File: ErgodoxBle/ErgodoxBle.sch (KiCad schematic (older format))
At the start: 86 parts, among them K0 KEYSW, K1 KEYSW, K10 KEYSW, K11 KEYSW, K12 KEYSW, K13 KEYSW, K14 KEYSW, K15 KEYSW, K16 KEYSW, K2 KEYSW, K20 KEYSW, K21 KEYSW, K22 KEYSW, K23 KEYSW, K24 KEYSW, K25 KEYSW, K26 KEYSW, K3 KEYSW, K30 KEYSW, K31 KEYSW, K32 KEYSW, K33 KEYSW, K34 KEYSW, K35 KEYSW, K36 KEYSW, K4 KEYSW, K40 KEYSW, K41 KEYSW, K42 KEYSW, K43 KEYSW, K44 KEYSW, K45 KEYSW, K46 KEYSW, K5 KEYSW, K54 KEYSW, K55 KEYSW, K56 KEYSW, K6 KEYSW, SW1 SW_PUSH, SW2 SW_PUSH

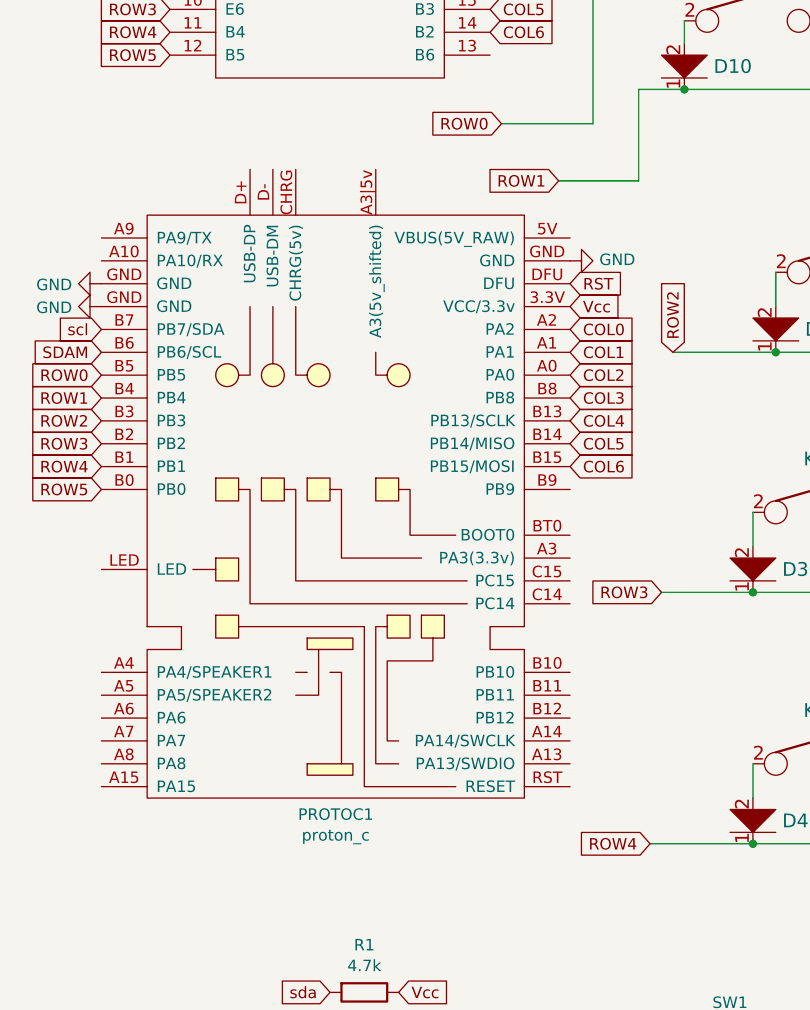
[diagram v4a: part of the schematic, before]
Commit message: added clearence for ProtonC
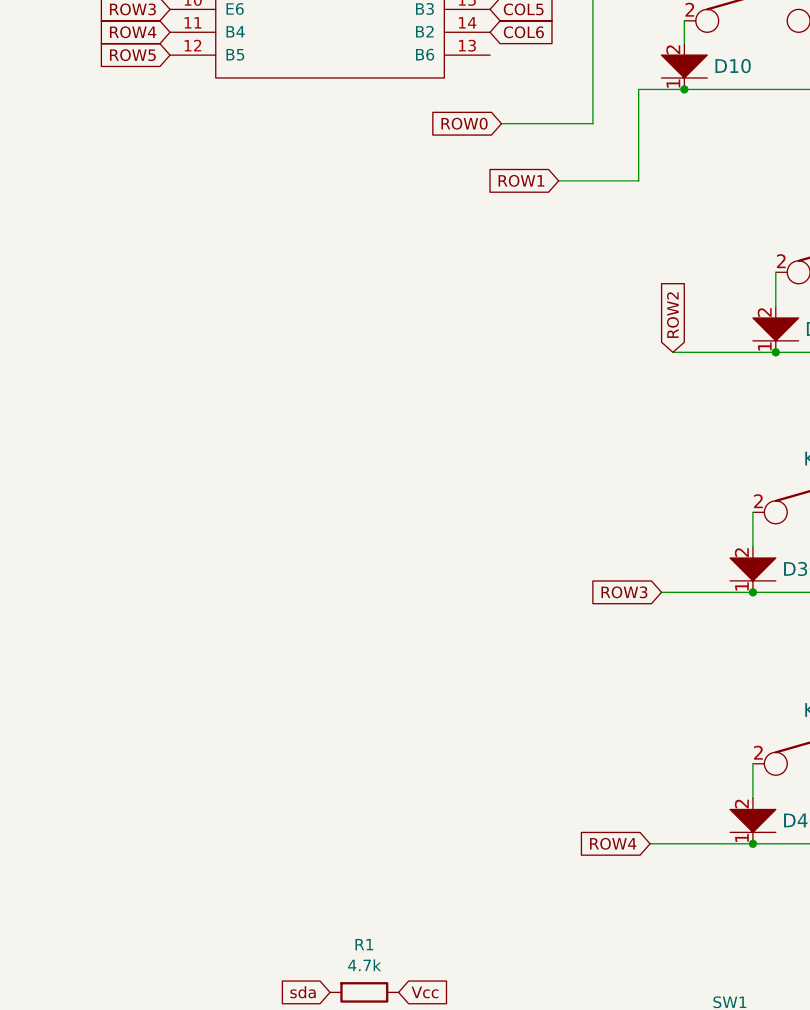
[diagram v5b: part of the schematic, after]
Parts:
- removed PROTOC1: proton_c, protonc:proton_c, symbol proton_c:proton_c
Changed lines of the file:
@@
 Text GLabel 10450 3900 0    50   Input ~ 0
 SDAM
-$Comp
-L proton_c:proton_c PROTOC1
-U 1 1 5C456AFA
-P 1550 3650
-F 0 "PROTOC1" H 1525 2128 50  0000 C CNN
-F 1 "proton_c" H 1525 2037 50  0000 C CNN
-F 2 "protonc:proton_c" H 1400 3650 50  0001 C CNN
-F 3 "" H 1400 3650 50  0001 C CNN
-	1    1550 3650
-	1    0    0    -1
-$EndComp
-Text GLabel 500  3250 0    50   Input ~ 0
-ROW0
-Text GLabel 500  3350 0    50   Input ~ 0
-ROW1
-Text GLabel 500  3450 0    50   Input ~ 0
-ROW2
-Text GLabel 500  3550 0    50   Input ~ 0
-ROW3
-Text GLabel 500  3650 0    50   Input ~ 0
-ROW4
-Text GLabel 500  3750 0    50   Input ~ 0
-ROW5
-Text GLabel 2550 3050 2    50   Input ~ 0
-COL0
-Text GLabel 2550 3150 2    50   Input ~ 0
-COL1
-Text GLabel 2550 3250 2    50   Input ~ 0
-COL2
-Text GLabel 2550 3350 2    50   Input ~ 0
-COL3
-Text GLabel 2550 3450 2    50   Input ~ 0
-COL4
-Text GLabel 2550 3550 2    50   Input ~ 0
-COL5
-Text GLabel 2550 3650 2    50   Input ~ 0
-COL6
-Text GLabel 2550 2850 2    50   Input ~ 0
-RST
-Text GLabel 2550 2950 2    50   Input ~ 0
-Vcc
-Text GLabel 500  3150 0    50   Input ~ 0
-SDAM
-Text GLabel 500  3050 0    50   Input ~ 0
-scl
-$Comp
-L power:GND #PWR0107
-U 1 1 5C45843C
-P 2550 2750
-F 0 "#PWR0107" H 2550 2500 50  0001 C CNN
-F 1 "GND" V 2555 2622 50  0000 R CNN
-F 2 "" H 2550 2750 50  0001 C CNN
-F 3 "" H 2550 2750 50  0001 C CNN
-	1    2550 2750
-	0    -1   -1   0
-$EndComp
-$Comp
-L power:GND #PWR0108
-U 1 1 5C45F50C
-P 500 2850
-F 0 "#PWR0108" H 500 2600 50  0001 C CNN
-F 1 "GND" V 505 2722 50  0000 R CNN
-F 2 "" H 500 2850 50  0001 C CNN
-F 3 "" H 500 2850 50  0001 C CNN
-	1    500  2850
-	0    1    1    0
-$EndComp
-$Comp
-L power:GND #PWR0109
-U 1 1 5C47B2A2
-P 500 2950
-F 0 "#PWR0109" H 500 2700 50  0001 C CNN
-F 1 "GND" V 505 2822 50  0000 R CNN
-F 2 "" H 500 2950 50  0001 C CNN
-F 3 "" H 500 2950 50  0001 C CNN
-	1    500  2950
-	0    1    1    0
-$EndComp
 $EndSCHEMATC

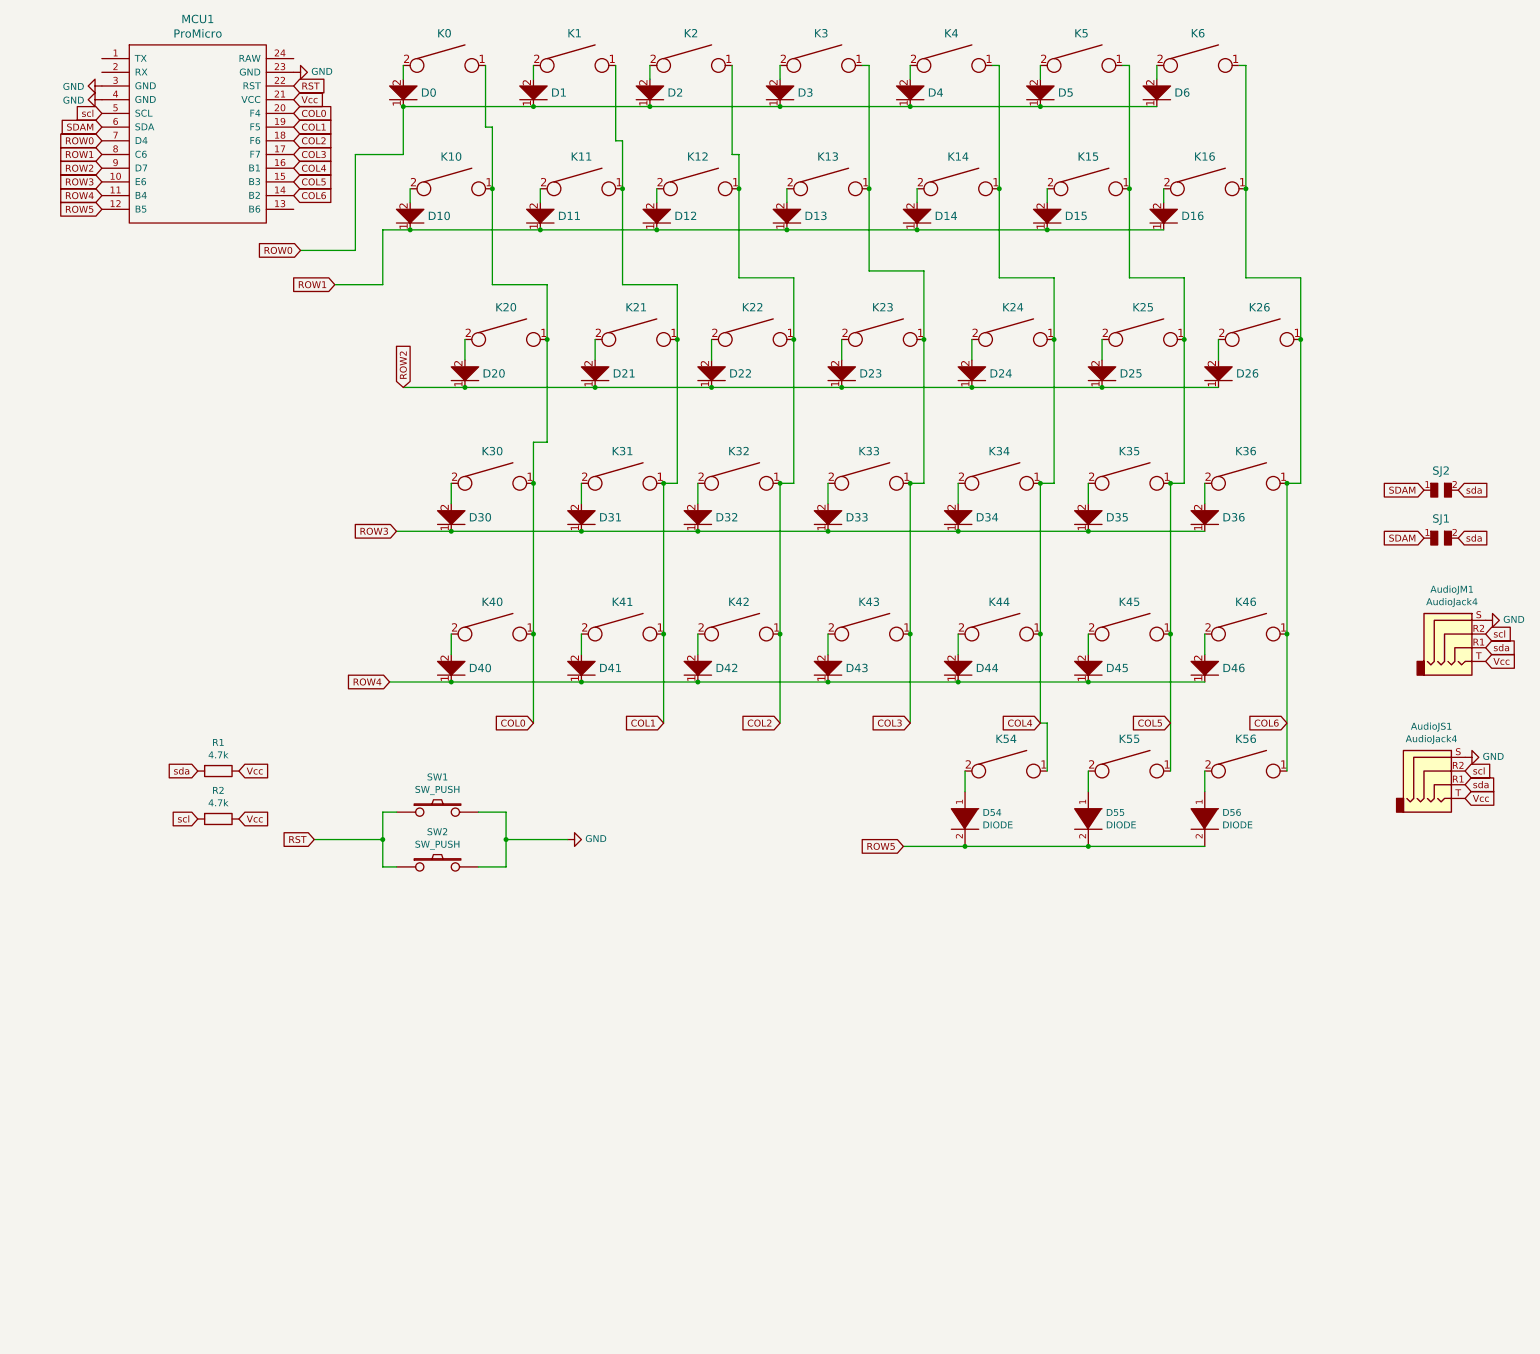
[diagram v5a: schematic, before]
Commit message: Redo the existing ergodox pcb
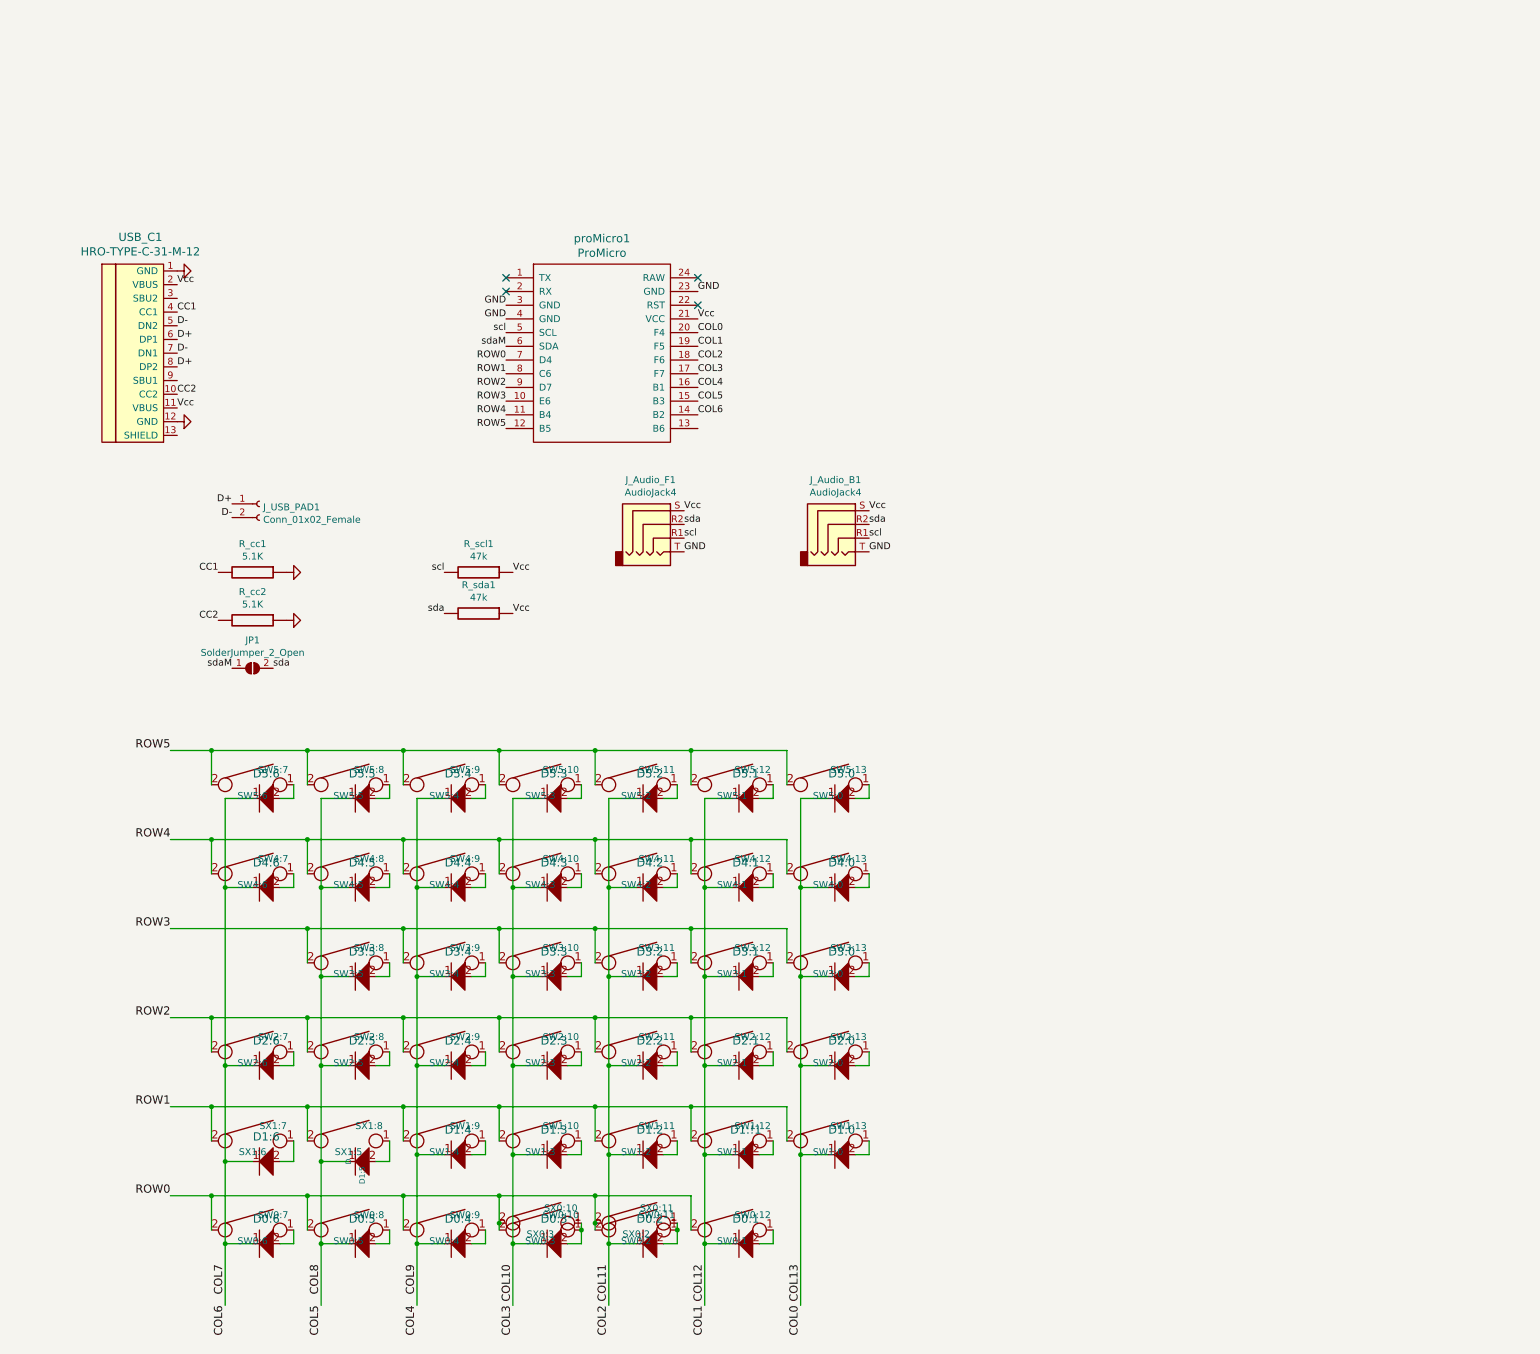
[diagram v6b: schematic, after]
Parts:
- removed AudioJM1, AudioJS1: AudioJack4, Connector_Audio:Jack_3.5mm_PJ320D_Horizontal, symbol Connector:AudioJack4
- removed D0, D1, D10, D11, D12, D13, D14, D15, D16, D2, D20, D21, D22, D23, D24, D25, D26, D3, D30, D31, D32, D33, D34, D35, D36, D4, D40, D41, D42, D43, D44, D45, D46, D5, D6: D, Keebio-Parts:Diode-dual, symbol keyboard_parts:D
- removed D54, D55, D56: DIODE, Keebio-Parts:Diode-dual, symbol pspice:DIODE
- removed K0, K1, K10, K11, K12, K13, K14, K15, K16, K2, K20, K21, K22, K23, K24, K25, K26, K3, K30, K31, K32, K33, K34, K35, K36, K4, K40, K41, K42, K43, K44, K45, K46, K5, K6: KEYSW, footprints:Mx_Alps_100-dualside, symbol keyboard_parts:KEYSW
- removed K54, K55: KEYSW, footprints:Mx_Alps_200-dualside, symbol canadian_parts:KEYSW
- removed K56: KEYSW, footprints:Mx_Alps_100-dualside, symbol canadian_parts:KEYSW
- removed MCU1: ProMicro, Keebio-Parts:ArduinoProMicro, symbol promicro:ProMicro
- removed R1, R2: 4.7k, Keebio-Parts:Resistor-Hybrid, symbol Device:R
- removed SJ1, SJ2: SOLDER_JUMPER, Keebio-Parts:solder_jumper, symbol keyboard_parts:SOLDER_JUMPER
- removed SW1, SW2: SW_PUSH, Button_Switch_SMD:SW_SPST_TL3342, symbol keyboard_parts2:SW_PUSH
- added D0:1, D0:2, D0:3, D0:4, D0:5, D0:6, D1:!1, D1:0, D1:2, D1:3, D1:4, D1:5, D1:6, D2:0, D2:1, D2:2, D2:3, D2:4, D2:5, D2:6, D3:0, D3:1, D3:2, D3:3, D3:4, D3:5, D4:0, D4:1, D4:2, D4:3, D4:4, D4:5, D4:6, D5:0, D5:1, D5:2, D5:3, D5:4, D5:5, D5:6: D, Keebio-Parts:Diode-dual, symbol keyboard_parts:D
- added JP1: SolderJumper_2_Open, Keebio-Parts:solder_jumper, symbol Jumper:SolderJumper_2_Open
- added J_Audio_B1, J_Audio_F1: AudioJack4, Connector_Audio:Jack_3.5mm_PJ320D_Horizontal, symbol Connector:AudioJack4
- added J_USB_PAD1: Conn_01x02_Female, Connector_Wire:SolderWirePad_1x02_P3.81mm_Drill0.8mm, symbol Connector:Conn_01x02_Female
- added R_cc1, R_cc2: 5.1K, Keebio-Parts:Resistor-Hybrid, symbol component:RESISTOR
- added R_scl1, R_sda1: 47k, Keebio-Parts:Resistor-Hybrid, symbol component:RESISTOR
- added SW0:10: SW0:3, Keebio-Parts:Hybrid_PCB_100H_Dual_hole, symbol canadian_parts:KEYSW
- added SW0:11: SW0:2, Keebio-Parts:Hybrid_PCB_100H_Dual_hole, symbol canadian_parts:KEYSW
- added SW0:12: SW0:1, Keebio-Parts:Hybrid_PCB_100H_Dual_hole, symbol canadian_parts:KEYSW
- added SW0:7: SW0:6, Keebio-Parts:Hybrid_PCB_100H_Dual_hole, symbol canadian_parts:KEYSW
- added SW0:8: SW0:5, Keebio-Parts:Hybrid_PCB_100H_Dual_hole, symbol canadian_parts:KEYSW
- added SW0:9: SW0:4, Keebio-Parts:Hybrid_PCB_100H_Dual_hole, symbol canadian_parts:KEYSW
- added SW1:10: SW1:3, Keebio-Parts:Hybrid_PCB_100H_Dual_hole, symbol canadian_parts:KEYSW
- added SW1:11: SW1:2, Keebio-Parts:Hybrid_PCB_100H_Dual_hole, symbol canadian_parts:KEYSW
- added SW1:12: SW1:1, Keebio-Parts:Hybrid_PCB_100H_Dual_hole, symbol canadian_parts:KEYSW
- added SW1:13: SW1:0, Keebio-Parts:Hybrid_PCB_100H_Dual_hole, symbol canadian_parts:KEYSW
- added SW1:9: SW1:4, Keebio-Parts:Hybrid_PCB_100H_Dual_hole, symbol canadian_parts:KEYSW
- added SW2:10: SW2:3, Keebio-Parts:Hybrid_PCB_100H_Dual_hole, symbol canadian_parts:KEYSW
- added SW2:11: SW2:2, Keebio-Parts:Hybrid_PCB_100H_Dual_hole, symbol canadian_parts:KEYSW
- added SW2:12: SW2:1, Keebio-Parts:Hybrid_PCB_100H_Dual_hole, symbol canadian_parts:KEYSW
- added SW2:13: SW2:0, Keebio-Parts:Hybrid_PCB_100H_Dual_hole, symbol canadian_parts:KEYSW
- added SW2:7: SW2:6, Keebio-Parts:Hybrid_PCB_100H_Dual_hole, symbol canadian_parts:KEYSW
- added SW2:8: SW2:5, Keebio-Parts:Hybrid_PCB_100H_Dual_hole, symbol canadian_parts:KEYSW
- added SW2:9: SW2:4, Keebio-Parts:Hybrid_PCB_100H_Dual_hole, symbol canadian_parts:KEYSW
- added SW3:10: SW3:3, Keebio-Parts:Hybrid_PCB_100H_Dual_hole, symbol canadian_parts:KEYSW
- added SW3:11: SW3:2, Keebio-Parts:Hybrid_PCB_100H_Dual_hole, symbol canadian_parts:KEYSW
- added SW3:12: SW3:1, Keebio-Parts:Hybrid_PCB_100H_Dual_hole, symbol canadian_parts:KEYSW
- added SW3:13: SW3:0, Keebio-Parts:Hybrid_PCB_100H_Dual_hole, symbol canadian_parts:KEYSW
- added SW3:8: SW3:5, Keebio-Parts:Hybrid_PCB_100H_Dual_hole, symbol canadian_parts:KEYSW
- added SW3:9: SW3:4, Keebio-Parts:Hybrid_PCB_100H_Dual_hole, symbol canadian_parts:KEYSW
- added SW4:10: SW4:3, Keebio-Parts:Hybrid_PCB_100H_Dual_hole, symbol canadian_parts:KEYSW
- added SW4:11: SW4:2, Keebio-Parts:Hybrid_PCB_100H_Dual_hole, symbol canadian_parts:KEYSW
- added SW4:12: SW4:1, Keebio-Parts:Hybrid_PCB_100H_Dual_hole, symbol canadian_parts:KEYSW
- added SW4:13: SW4:0, Keebio-Parts:Hybrid_PCB_100H_Dual_hole, symbol canadian_parts:KEYSW
- added SW4:7: SW4:6, Keebio-Parts:Hybrid_PCB_100H_Dual_hole, symbol canadian_parts:KEYSW
- added SW4:8: SW4:5, Keebio-Parts:Hybrid_PCB_100H_Dual_hole, symbol canadian_parts:KEYSW
- added SW4:9: SW4:4, Keebio-Parts:Hybrid_PCB_100H_Dual_hole, symbol canadian_parts:KEYSW
- added SW5:10: SW5:3, Keebio-Parts:Hybrid_PCB_100H_Dual_hole, symbol canadian_parts:KEYSW
- added SW5:11: SW5:2, Keebio-Parts:Hybrid_PCB_100H_Dual_hole, symbol canadian_parts:KEYSW
- added SW5:12: SW5:1, Keebio-Parts:Hybrid_PCB_100H_Dual_hole, symbol canadian_parts:KEYSW
- added SW5:13: SW5:0, Keebio-Parts:Hybrid_PCB_100H_Dual_hole, symbol canadian_parts:KEYSW
- added SW5:7: SW5:6, Keebio-Parts:Hybrid_PCB_100H_Dual_hole, symbol canadian_parts:KEYSW
- added SW5:8: SW5:5, Keebio-Parts:Hybrid_PCB_100H_Dual_hole, symbol canadian_parts:KEYSW
- added SW5:9: SW5:4, Keebio-Parts:Hybrid_PCB_100H_Dual_hole, symbol canadian_parts:KEYSW
- added SX0:10: SX0:3, Keebio-Parts:Hybrid_PCB_100H_Dual_hole, symbol canadian_parts:KEYSW
- added SX0:11: SX0:2, Keebio-Parts:Hybrid_PCB_100H_Dual_hole, symbol canadian_parts:KEYSW
- added SX1:7: SX1:6, Keebio-Parts:Hybrid_PCB_100H_Dual_hole, symbol canadian_parts:KEYSW
- added SX1:8: SX1:5, Keebio-Parts:Hybrid_PCB_100H_Dual_hole, symbol canadian_parts:KEYSW
- added USB_C1: HRO-TYPE-C-31-M-12, usbc_footprint:HRO-TYPE-C-31-M-12, symbol Type-C:HRO-TYPE-C-31-M-12
- added proMicro1: ProMicro, Keebio-Parts:ArduinoProMicro, symbol promicro:ProMicro
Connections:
- net COL0: now also D1:0.1, D2:0.1, D3:0.1, D4:0.1, D5:0.1, proMicro1.20 (F4)
- net COL1: now also D0:1.1, D1:!1.1, D2:1.1, D3:1.1, D4:1.1, D5:1.1, proMicro1.19 (F5)
- net COL4: now also D0:4.1, D1:4.1, D2:4.1, D3:4.1, D4:4.1, D5:4.1, proMicro1.16 (B1)
- net COL5: now also D0:5.1, D1:5.1, D2:5.1, D3:5.1, D4:5.1, D5:5.1, proMicro1.15 (B3)
- net COL6: now also D0:6.1, D1:6.1, D2:6.1, D4:6.1, D5:6.1, proMicro1.14 (B2)
- net GND: now also J_Audio_B1.T, J_Audio_F1.T, R_cc1.1, R_cc2.1, USB_C1.1 (GND), USB_C1.12 (GND), proMicro1.23 (GND), proMicro1.3 (GND), proMicro1.4 (GND)
- net ROW0: now also SW0:10.2, SW0:11.2, SW0:12.2, SW0:7.2, SW0:8.2, SW0:9.2, SX0:10.2, SX0:11.2, proMicro1.7 (D4)
- net ROW1: now also SW1:10.2, SW1:11.2, SW1:12.2, SW1:13.2, SW1:9.2, SX1:7.2, SX1:8.2, proMicro1.8 (C6)
- net ROW2: now also SW2:10.2, SW2:11.2, SW2:12.2, SW2:13.2, SW2:7.2, SW2:8.2, SW2:9.2, proMicro1.9 (D7)
- net ROW3: now also SW3:10.2, SW3:11.2, SW3:12.2, SW3:13.2, SW3:8.2, SW3:9.2, proMicro1.10 (E6)
- net ROW4: now also SW4:10.2, SW4:11.2, SW4:12.2, SW4:13.2, SW4:7.2, SW4:8.2, SW4:9.2, proMicro1.11 (B4)
- net ROW5: now also SW5:10.2, SW5:11.2, SW5:12.2, SW5:13.2, SW5:7.2, SW5:8.2, SW5:9.2, proMicro1.12 (B5)
- net Vcc: now also J_Audio_B1.S, J_Audio_F1.S, R_scl1.1, R_sda1.1, USB_C1.11 (VBUS), USB_C1.2 (VBUS), proMicro1.21 (VCC)
- net scl: now also J_Audio_B1.R1, J_Audio_F1.R1, R_scl1.2, proMicro1.5 (SCL)
- net sda: now also JP1.2 (B), J_Audio_B1.R2, J_Audio_F1.R2, R_sda1.2
- new net: D0:3.2, SW0:10.1, SX0:10.1
- new net: D4:6.2, SW4:7.1
- new net: D4:5.2, SW4:8.1
- new net: D4:1.2, SW4:12.1
- new net: D4:2.2, SW4:11.1
- new net: D4:3.2, SW4:10.1
- new net: D4:4.2, SW4:9.1
- new net: D4:0.2, SW4:13.1
- new net: D3:1.2, SW3:12.1
- new net: D3:2.2, SW3:11.1
- new net: D3:3.2, SW3:10.1
- new net: D3:4.2, SW3:9.1
- new net: D3:5.2, SW3:8.1
- new net: D1:4.2, SW1:9.1
- new net: D1:3.2, SW1:10.1
- new net: D1:!1.2, SW1:12.1
- new net: D2:1.2, SW2:12.1
- new net: D2:2.2, SW2:11.1
- new net: D2:3.2, SW2:10.1
- new net: D2:4.2, SW2:9.1
- new net: D2:5.2, SW2:8.1
- new net: D2:6.2, SW2:7.1
- new net: D3:0.2, SW3:13.1
- new net: D1:0.2, SW1:13.1
- new net: D2:0.2, SW2:13.1
- new net: D0:2.2, SW0:11.1, SX0:11.1
- new net: D0:1.2, SW0:12.1
- new net: D0:6.2, SW0:7.1
- new net: D0:5.2, SW0:8.1
- new net: D0:4.2, SW0:9.1
- new net: D1:2.2, SW1:11.1
- new net: D5:0.2, SW5:13.1
- new net: D5:4.2, SW5:9.1
- new net: D5:3.2, SW5:10.1
- new net: D5:2.2, SW5:11.1
- new net: D5:1.2, SW5:12.1
- new net: D5:5.2, SW5:8.1
- new net: D5:6.2, SW5:7.1
- new net: D1:5.2, SX1:8.1
- new net: D1:6.2, SX1:7.1
- new net CC1: R_cc1.2, USB_C1.4 (CC1)
- new net CC2: R_cc2.2, USB_C1.10 (CC2)
- new net COL10: D0:3.1, D1:3.1, D2:3.1, D3:3.1, D4:3.1, D5:3.1, proMicro1.17 (F7)
- new net COL11: D0:2.1, D1:2.1, D2:2.1, D3:2.1, D4:2.1, D5:2.1, proMicro1.18 (F6)
- new net D+: J_USB_PAD1.1 (Pin_1), USB_C1.6 (DP1), USB_C1.8 (DP2)
- new net D-: J_USB_PAD1.2 (Pin_2), USB_C1.5 (DN2), USB_C1.7 (DN1)
- new net sdaM: JP1.1 (A), proMicro1.6 (SDA)
- no-connect marks 0 -> 4

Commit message: schema and pcb pdf
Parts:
- added U_VR_IC1: AMS1117-3.3, Package_TO_SOT_SMD:SOT-223-3_TabPin2, symbol Regulator_Linear:AMS1117-3.3
- J_Audio_B1, J_Audio_F1: footprint Connector_Audio:Jack_3.5mm_PJ320D_Horizontal -> Keebio-Parts:TRRS-PJ-320D
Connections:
- net GND: now also U_VR_IC1.1 (GND)
- net Vcc: now also U_VR_IC1.2 (VO); no longer USB_C1.11 (VBUS), USB_C1.2 (VBUS)
- new net VccR: USB_C1.11 (VBUS), USB_C1.2 (VBUS), U_VR_IC1.3 (VI)
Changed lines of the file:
@@
 EESchema Schematic File Version 4
-LIBS:component
-LIBS:ErgoDOX-cache
+LIBS:ErgodoxBle-cache
 EELAYER 26 0
 EELAYER END
@@
 F 0 "J_Audio_F1" H 4805 4475 50  0000 C CNN
 F 1 "AudioJack4" H 4805 4384 50  0000 C CNN
-F 2 "Connector_Audio:Jack_3.5mm_PJ320D_Horizontal" H 4850 4150 50  0001 C CNN
+F 2 "Keebio-Parts:TRRS-PJ-320D" H 4850 4150 50  0001 C CNN
 F 3 "~" H 4850 4150 50  0001 C CNN
 	1    4850 4150
@@
 F 0 "J_Audio_B1" H 6155 4475 50  0000 C CNN
 F 1 "AudioJack4" H 6155 4384 50  0000 C CNN
-F 2 "Connector_Audio:Jack_3.5mm_PJ320D_Horizontal" H 6200 4150 50  0001 C CNN
+F 2 "Keebio-Parts:TRRS-PJ-320D" H 6200 4150 50  0001 C CNN
 F 3 "~" H 6200 4150 50  0001 C CNN
 	1    6200 4150
@@
 $EndComp
 Text Label 1350 2400 0    50   ~ 0
-Vcc
+VccR
 Text Label 1350 2600 0    50   ~ 0
 CC1
@@
 $EndComp
 Text Label 1350 3300 0    50   ~ 0
-Vcc
+VccR
 Text Label 1350 2700 0    50   ~ 0
 D-
@@
 Text Label 1350 3000 0    50   ~ 0
 D+
+$Comp
+L Regulator_Linear:AMS1117-3.3 U_VR_IC1
+U 1 1 5C499923
+P 2050 1400
+F 0 "U_VR_IC1" H 2050 1642 50  0000 C CNN
+F 1 "AMS1117-3.3" H 2050 1551 50  0000 C CNN
+F 2 "Package_TO_SOT_SMD:SOT-223-3_TabPin2" H 2050 1600 50  0001 C CNN
+F 3 "http://www.advanced-monolithic.com/pdf/ds1117.pdf" H 2150 1150 50  0001 C CNN
+	1    2050 1400
+	1    0    0    -1
+$EndComp
+Text Label 1750 1400 2    50   ~ 0
+VccR
+Text Label 2350 1400 0    50   ~ 0
+Vcc
+$Comp
+L component:GND #PWR0105
+U 1 1 5C49AE71
+P 2050 1750
+F 0 "#PWR0105" H 2050 1750 30  0001 C CNN
+F 1 "GND" H 2050 1680 30  0001 C CNN
+F 2 "" H 2050 1750 50  0001 C CNN
+F 3 "" H 2050 1750 50  0001 C CNN
+	1    2050 1750
+	1    0    0    -1
+$EndComp
 $EndSCHEMATC
